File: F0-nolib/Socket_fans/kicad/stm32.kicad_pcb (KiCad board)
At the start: 2 copper layers, 93.5 x 55 mm, 67 parts, among them J1 A, J10 12v, J11 DB9_Male, J12 RS-485, J13 Conn_01x06, J2 B, J3 Conn_01x08_Female, J4 Conn_01x08_Female, J5 +/-, J6 CONN_02X03, J7 0/1, J8 2/3, J9 DB9_Female, P1 USB_A, P2 Hole, P3 Hole, P4 Hole, P5 Hole, Q1 SI2305, Q2 AO3407, SW1 SW_DIP_x01, U2 LM1117-5.0, U3 LM1117-3.3, U4 MCP2551-I/SN, U5 STM32F072CBTx, U6 MAX3485

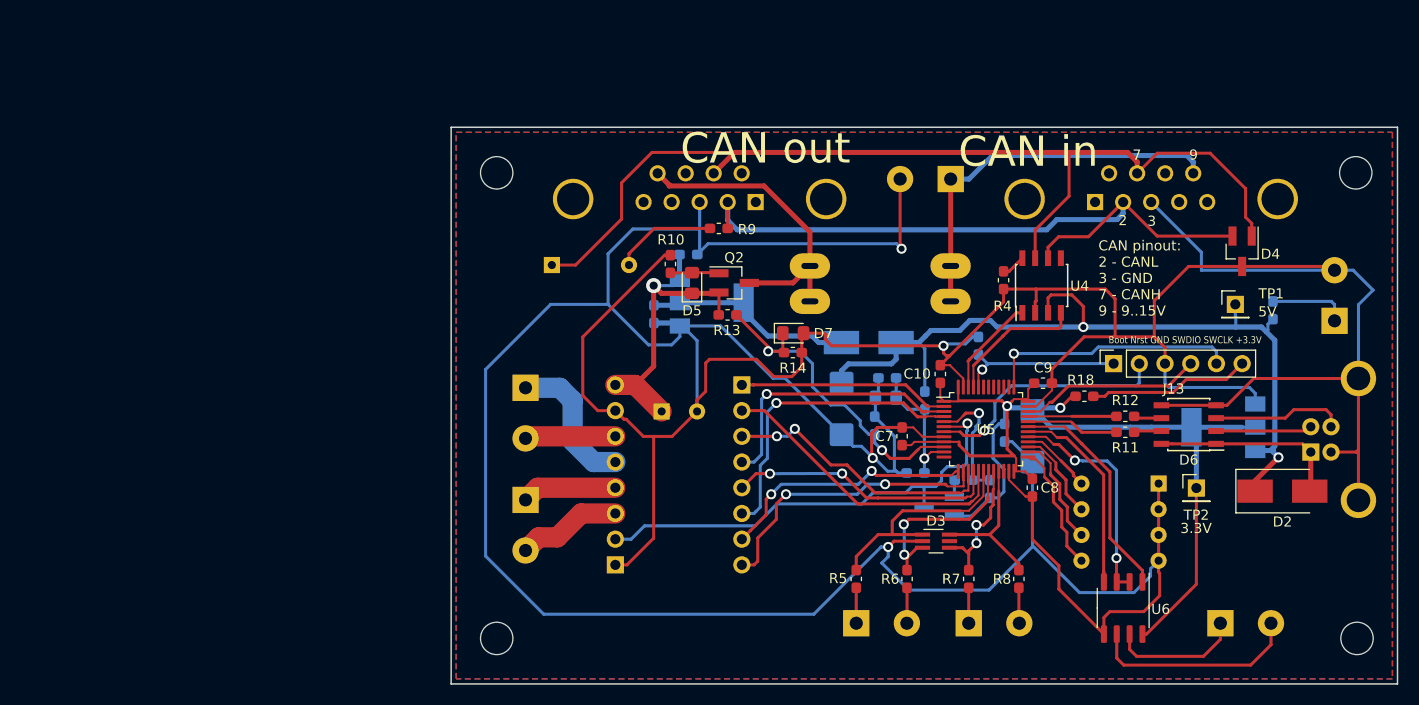
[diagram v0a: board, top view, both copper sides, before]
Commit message: add socket_fans PCB
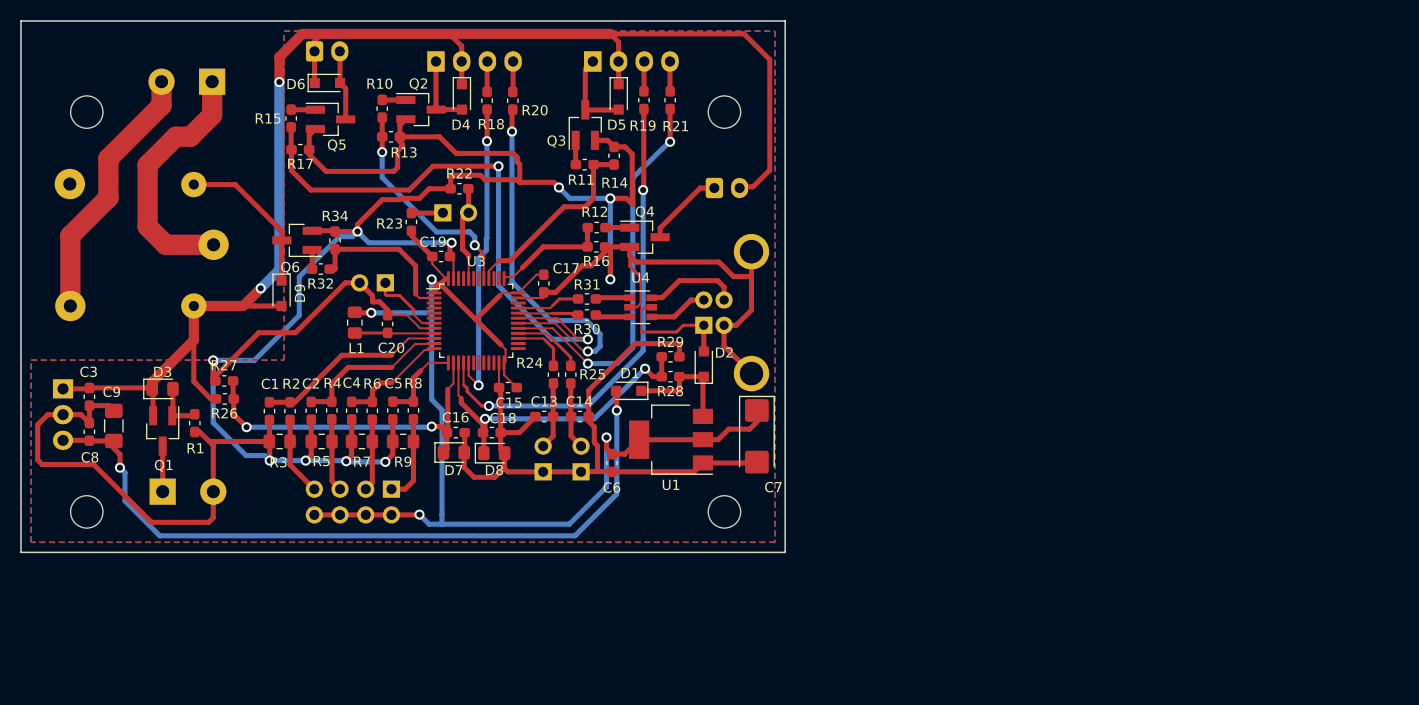
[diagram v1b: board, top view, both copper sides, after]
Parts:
- removed C10, C11, C12: 0.1, Capacitor_SMD:C_0603_1608Metric_Pad1.05x0.95mm_HandSolder
- removed F1: 1A, MyFootprints:FuseHolder
- removed J11: DB9_Male, Connector_Dsub:DSUB-9_Male_Horizontal_P2.77x2.84mm_EdgePinOffset4.94mm_Housed_MountingHolesOffset7.48mm
- removed J12: RS-485, TerminalBlock_Phoenix:TerminalBlock_Phoenix_MKDS-1,5-2_1x02_P5.00mm_Horizontal
- removed J13: Conn_01x06, Connector_PinSocket_2.54mm:PinSocket_1x06_P2.54mm_Vertical
- removed J9: DB9_Female, Connector_Dsub:DSUB-9_Female_Horizontal_P2.77x2.84mm_EdgePinOffset4.94mm_Housed_MountingHolesOffset7.48mm
- removed TP1, TP2: TestPoint, Connector_PinHeader_2.54mm:PinHeader_1x01_P2.54mm_Vertical
- removed U5: STM32F072CBTx, Package_QFP:LQFP-48_7x7mm_P0.5mm
- removed U6: MAX3485, Package_SO:SO-8_3.9x4.9mm_P1.27mm
- added C13: 0.1, Capacitor_SMD:C_0603_1608Metric_Pad1.05x0.95mm_HandSolder, F.Cu at (89.7, 91.1)
- added C14: 0.1, Capacitor_SMD:C_0603_1608Metric_Pad1.05x0.95mm_HandSolder, F.Cu at (93.2, 91.1)
- added C15: 0.1, Capacitor_SMD:C_0603_1608Metric_Pad1.05x0.95mm_HandSolder, F.Cu at (86.1, 88.2)
- added C16: 0.1, Capacitor_SMD:C_0603_1608Metric_Pad1.05x0.95mm_HandSolder, F.Cu at (81.0, 92.7)
- added C17: 0.1, Capacitor_SMD:C_0603_1608Metric_Pad1.05x0.95mm_HandSolder, F.Cu at (89.7, 77.9)
- added C18: 0.1, Capacitor_SMD:C_0603_1608Metric_Pad1.05x0.95mm_HandSolder, F.Cu at (84.5, 92.7)
- added C19: 0.1, Capacitor_SMD:C_0603_1608Metric_Pad1.05x0.95mm_HandSolder, F.Cu at (79.5, 75.3)
- added C20: 0.1, Capacitor_SMD:C_0603_1608Metric_Pad1.05x0.95mm_HandSolder, F.Cu at (74.2, 81.9)
- added D9: 1N5819, Diode_SMD:D_SOD-323_HandSoldering, F.Cu at (63.7, 78.9)
- added K1: SRD-12VDC, Relay_THT:Relay_SPDT_SANYOU_SRD_Series_Form_C, B.Cu at (57.0, 74.1)
- added L1: BMBA 0.1mH, Inductor_SMD:L_0805_2012Metric_Pad1.15x1.40mm_HandSolder, F.Cu at (71.0, 81.8)
- added Q3: IRLML2502, Package_TO_SOT_SMD:SOT-23_Handsoldering, F.Cu at (93.8, 62.3)
- added Q4: IRLML2502, Package_TO_SOT_SMD:SOT-23_Handsoldering, F.Cu at (99.6, 73.4)
- added Q5: IRLML2502, Package_TO_SOT_SMD:SOT-23_Handsoldering, F.Cu at (68.6, 61.7)
- added Q6: IRLML2502, Package_TO_SOT_SMD:SOT-23_Handsoldering, F.Cu at (65.3, 73.7)
- added R19: 510, Resistor_SMD:R_0603_1608Metric_Pad1.05x0.95mm_HandSolder, F.Cu at (99.5, 59.8)
- added R20: 510, Resistor_SMD:R_0603_1608Metric_Pad1.05x0.95mm_HandSolder, F.Cu at (86.6, 59.9)
- added R21: 510, Resistor_SMD:R_0603_1608Metric_Pad1.05x0.95mm_HandSolder, F.Cu at (102.1, 59.8)
- added R22: 47k, Resistor_SMD:R_0603_1608Metric_Pad1.05x0.95mm_HandSolder, F.Cu at (81.3, 68.6)
- added R23: 22, Resistor_SMD:R_0603_1608Metric_Pad1.05x0.95mm_HandSolder, F.Cu at (76.6, 71.9)
- added R24: 510, Resistor_SMD:R_0603_1608Metric_Pad1.05x0.95mm_HandSolder, F.Cu at (90.6, 86.9)
- added R25: 510, Resistor_SMD:R_0603_1608Metric_Pad1.05x0.95mm_HandSolder, F.Cu at (92.3, 86.9)
- added R26: 220k, Resistor_SMD:R_0603_1608Metric_Pad1.05x0.95mm_HandSolder, F.Cu at (58.1, 89.3)
- added R27: 56k, Resistor_SMD:R_0603_1608Metric_Pad1.05x0.95mm_HandSolder, F.Cu at (58.1, 87.6)
- added R28: 47k, Resistor_SMD:R_0603_1608Metric_Pad1.05x0.95mm_HandSolder, F.Cu at (102.2, 87.1)
- added R29: 47k, Resistor_SMD:R_0603_1608Metric_Pad1.05x0.95mm_HandSolder, F.Cu at (102.2, 85.2)
- added R30: 22, Resistor_SMD:R_0603_1608Metric_Pad1.05x0.95mm_HandSolder, F.Cu at (93.9, 81.0)
- added R31: 22, Resistor_SMD:R_0603_1608Metric_Pad1.05x0.95mm_HandSolder, F.Cu at (93.9, 79.5)
- added R32: 510, Resistor_SMD:R_0603_1608Metric_Pad1.05x0.95mm_HandSolder, F.Cu at (67.6, 76.5)
- added R34: 10k, Resistor_SMD:R_0603_1608Metric_Pad1.05x0.95mm_HandSolder, F.Cu at (69.0, 73.7)
- added SW2: SW_Push, Connector_PinSocket_2.54mm:PinSocket_1x02_P2.54mm_Vertical, B.Cu at (93.3, 96.5)
- added U1: LM1117-3.3, Package_TO_SOT_SMD:SOT-223-3_TabPin2, F.Cu at (102.2, 93.4)
- C1, C3, C5, R2: moved to F.Cu
- C2: value 100uF -> 0.1; footprint Capacitor_THT:CP_Radial_D8.0mm_P3.50mm -> Capacitor_SMD:C_0603_1608Metric_Pad1.05x0.95mm_HandSolder; moved to F.Cu
- C4, C6: value 47uF, 10V -> 0.1; footprint Capacitor_Tantalum_SMD:CP_EIA-6032-28_Kemet-C_Pad2.25x2.35mm_HandSolder -> Capacitor_SMD:C_0603_1608Metric_Pad1.05x0.95mm_HandSolder; moved to F.Cu
- C7: value 0.1 -> 47uF, 10V; footprint Capacitor_SMD:C_0603_1608Metric_Pad1.05x0.95mm_HandSolder -> Capacitor_Tantalum_SMD:CP_EIA-6032-28_Kemet-C_Pad2.25x2.35mm_HandSolder
- C9: value 0.1 -> 10uF, 10V; footprint Capacitor_SMD:C_0603_1608Metric_Pad1.05x0.95mm_HandSolder -> Capacitor_SMD:C_1206_3216Metric_Pad1.42x1.75mm_HandSolder
- D1: value MBRS130L -> 1N5819; footprint Diode_SMD:D_SMB_Handsoldering -> Diode_SMD:D_SOD-323_HandSoldering; moved to F.Cu
- D2: value MBRS130L -> 1N5819; footprint Diode_SMD:D_SMB_Handsoldering -> Diode_SMD:D_SOD-323_HandSoldering
- D3: value PESD3V3L4UG -> MM3Z7V5; footprint TO_SOT_Packages_SMD:SOT-363_SC-70-6_Handsoldering -> Diode_SMD:D_0805_2012Metric_Pad1.15x1.40mm_HandSolder
- D4: value PESD1CAN -> 1N5819; footprint TO_SOT_Packages_SMD:SOT-23_Handsoldering -> Diode_SMD:D_SOD-323_HandSoldering
- D5: value MM3Z7V5 -> 1N5819; footprint Diode_SMD:D_0805_2012Metric_Pad1.15x1.40mm_HandSolder -> Diode_SMD:D_SOD-323_HandSoldering
- D6: value USB6B1 -> 1N5819; footprint Package_SO:SOIC-8_3.9x4.9mm_P1.27mm -> Diode_SMD:D_SOD-323_HandSoldering
- D7: value MM3Z3V9 -> MM3Z4V7
- D8: value MM3Z3V9 -> MM3Z4V7; moved to F.Cu
- J1: value A -> 12VIN
- J10: value 12v -> Conn_01x02_Female; footprint TerminalBlock_Phoenix:TerminalBlock_Phoenix_MKDS-1,5-2_1x02_P5.00mm_Horizontal -> Connector_PinSocket_2.54mm:PinSocket_1x02_P2.54mm_Vertical
- J2: value B -> thermal; footprint TerminalBlock_Phoenix:TerminalBlock_Phoenix_MKDS-1,5-2_1x02_P5.00mm_Horizontal -> Connector_PinSocket_2.54mm:PinSocket_2x04_P2.54mm_Vertical
- J3: value Conn_01x08_Female -> Buzzer; footprint Connector_PinSocket_2.54mm:PinSocket_1x08_P2.54mm_Vertical -> Connector_JST:JST_EH_B2B-EH-A_1x02_P2.50mm_Vertical
- J4: value Conn_01x08_Female -> cooler3; footprint Connector_PinSocket_2.54mm:PinSocket_1x08_P2.54mm_Vertical -> Connector_JST:JST_EH_B2B-EH-A_1x02_P2.50mm_Vertical
- J5: value +/- -> FAN; footprint TerminalBlock_Phoenix:TerminalBlock_Phoenix_MKDS-1,5-2_1x02_P5.00mm_Horizontal -> Connector:FanPinHeader_1x04_P2.54mm_Vertical
- J6: value CONN_02X03 -> FAN; footprint Button_Switch_THT:SW_DIP_SPSTx04_Slide_9.78x12.34mm_W7.62mm_P2.54mm -> Connector:FanPinHeader_1x04_P2.54mm_Vertical
- J7: value 0/1 -> Conn_01x02_Female; footprint TerminalBlock_Phoenix:TerminalBlock_Phoenix_MKDS-1,5-2_1x02_P5.00mm_Horizontal -> Connector_PinSocket_2.54mm:PinSocket_1x02_P2.54mm_Vertical
- J8: value 2/3 -> MKDS
- P1: footprint Connectors_USB:USB_B_OST_USB-B1HSxx_Horizontal -> Connector_USB:USB_B_OST_USB-B1HSxx_Horizontal
- Q1: value SI2305 -> AO3401; footprint TO_SOT_Packages_SMD:SOT-23_Handsoldering -> Package_TO_SOT_SMD:SOT-23_Handsoldering; moved to F.Cu
- Q2: value AO3407 -> IRLML2502; footprint TO_SOT_Packages_SMD:SOT-23_Handsoldering -> Package_TO_SOT_SMD:SOT-23_Handsoldering
- R1: value 330 -> 10k; moved to F.Cu
- R10: value 10k -> 510
- R11, R12, R18: value 22 -> 510
- R13: value 220k -> 10k
- R14: value 56k -> 10k
- R15: value 47k -> 510; moved to F.Cu
- R16, R17: value 47k -> 10k; moved to F.Cu
- R3: value 120 -> 4k7, 1%; footprint Resistor_SMD:R_0603_1608Metric_Pad1.05x0.95mm_HandSolder -> Resistor_SMD:R_0805_2012Metric_Pad1.15x1.40mm_HandSolder; moved to F.Cu
- R4: value 15k -> 10k
- R5, R7: value 330 -> 4k7, 1%; footprint Resistor_SMD:R_0603_1608Metric_Pad1.05x0.95mm_HandSolder -> Resistor_SMD:R_0805_2012Metric_Pad1.15x1.40mm_HandSolder
- R6, R8: value 330 -> 10k
- R9: value 120 -> 4k7, 1%; footprint Resistor_SMD:R_0603_1608Metric_Pad1.05x0.95mm_HandSolder -> Resistor_SMD:R_0805_2012Metric_Pad1.15x1.40mm_HandSolder
- SW1: value SW_DIP_x01 -> SW_Push; footprint Button_Switch_THT:SW_DIP_SPSTx01_Slide_6.7x4.1mm_W7.62mm_P2.54mm_LowProfile -> Connector_PinSocket_2.54mm:PinSocket_1x02_P2.54mm_Vertical
- U2: value LM1117-5.0 -> L7805; footprint TO_SOT_Packages_SMD:SOT-223-3_TabPin2 -> Package_TO_SOT_THT:TO-220-3_Vertical
- U3: value LM1117-3.3 -> STM32F072CBTx; footprint TO_SOT_Packages_SMD:SOT-223-3_TabPin2 -> Package_QFP:LQFP-48_7x7mm_P0.5mm; moved to F.Cu
- U4: value MCP2551-I/SN -> USBLC6-2SC6; footprint Package_SO:SOIC-8_3.9x4.9mm_P1.27mm -> Package_TO_SOT_SMD:SOT-23-6
- moved P4 125.5 mm to (44.5, 61.0)
- moved R3 99.0 mm to (63.6, 93.5), turned to 0 degrees
- moved C8 93.3 mm to (44.8, 92.6)
- moved J5 92.4 mm to (79.0, 56.0), turned to 0 degrees
- moved J8 91.9 mm to (56.9, 58.0), turned to 180 degrees
- moved C9 91.9 mm to (47.2, 92.0), turned to 90 degrees
- moved D6 91.5 mm to (68.3, 58.1), turned to 0 degrees
- moved D4 78.6 mm to (81.6, 59.5)
- moved D3 77.9 mm to (52.0, 88.3)
- moved Q1 77.1 mm to (52.0, 92.5), turned to 270 degrees
- moved R1 76.2 mm to (55.2, 91.7), turned to 270 degrees
- moved U3 74.6 mm to (83.0, 81.6), turned to 0 degrees
- moved J6 69.7 mm to (94.5, 56.0), turned to 0 degrees
- moved R17 69.7 mm to (65.6, 64.7), turned to 180 degrees
- moved R2 69.6 mm to (64.6, 90.5)
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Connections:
- C1 pad 1: /12Vin -> GND
- C1 pad 2: GND -> /ADC0
- C2 pad 1: /12Vin -> GND
- C2 pad 2: GND -> /ADC1
- C3 pad 1: /5Vin -> +12V
- C4 pad 1: +5V -> GND
- C4 pad 2: GND -> /ADC2
- C5 pad 1: +3V3 -> GND
- C5 pad 2: GND -> /ADC3
- C7 pad 1: GND -> +3V3
- C7 pad 2: +3V3 -> GND
- C8 pad 1: GND -> /5Vin
- C8 pad 2: +3V3 -> GND
- C9 pad 1: GND -> /5Vin
- C9 pad 2: +3V3 -> GND
- D3 pad 1: /ESW0 -> +12V
- D3 pad 2: GND -> Net-(D3-Pad2)
- D4 pad 1: Net-(D4-Pad1) -> +12V
- D5 pad 1: /12Vin -> +12V
- D6 pad 1: /5Vusb -> +12V
- J1 pad 2: Net-(J1-Pad2) -> GND
- J10 pad 1: Net-(F1-Pad1) -> /NRST
- J2 pad 2: Net-(J2-Pad2) -> +3V3
- J3 pad 1: GND -> Net-(J3-Pad1)
- J3 pad 2: /~FAULT -> +12V
- J4 pad 1: /~EN -> +12V
- J4 pad 2: /MOSI -> Net-(D6-Pad2)
- J5 pad 1: Net-(J5-Pad1) -> Net-(D4-Pad2)
- J5 pad 2: GND -> +12V
- J6 pad 1: GND -> Net-(D5-Pad2)
- J6 pad 2: GND -> +12V
- J6 pad 3: GND -> Net-(J6-Pad3)
- J6 pad 4: GND -> Net-(J6-Pad4)
- J7 pad 2: Net-(J7-Pad2) -> /BOOT0
- P1 pad 2: Net-(D6-Pad2) -> Net-(P1-Pad2)
- P1 pad 3: Net-(D6-Pad3) -> Net-(P1-Pad3)
- Q1 pad 1: Net-(Q1-Pad1) -> Net-(D3-Pad2)
- Q1 pad 2: +3V3 -> +12V
- Q1 pad 3: /~FAULT -> Net-(J1-Pad1)
- Q2 pad 1: Net-(D5-Pad2) -> Net-(Q2-Pad1)
- Q2 pad 2: /12Vin -> GND
- Q2 pad 3: Net-(F1-Pad2) -> Net-(D4-Pad2)
- R1 pad 1: Net-(Q1-Pad1) -> Net-(D3-Pad2)
- R1 pad 2: /VIO_on -> GND
- R10 pad 1: Net-(D5-Pad2) -> Net-(Q2-Pad1)
- R10 pad 2: GND -> /Cooler1
- R11 pad 1: Net-(D6-Pad7) -> Net-(Q3-Pad1)
- R11 pad 2: Net-(R11-Pad2) -> /Cooler0
- R12 pad 1: Net-(D6-Pad6) -> Net-(Q4-Pad1)
- R12 pad 2: Net-(R12-Pad2) -> /Buzzer
- R13 pad 1: /12Vin -> GND
- R13 pad 2: /AIN0 -> /Cooler1
- R14 pad 1: /AIN0 -> GND
- R14 pad 2: GND -> /Cooler0
- R15 pad 1: +5V -> Net-(Q5-Pad1)
- R15 pad 2: /AIN1 -> /TIM1_CH3
- R16 pad 1: /AIN1 -> GND
- R16 pad 2: GND -> /Buzzer
- R17 pad 1: /BOOT0 -> GND
- R17 pad 2: GND -> /TIM1_CH3
- R18 pad 1: Net-(J13-Pad6) -> /TIM14_CH1
- R18 pad 2: +3V3 -> Net-(J5-Pad3)
- R2 pad 1: +3V3 -> Net-(J2-Pad7)
- R2 pad 2: /VIO_on -> /ADC0
- R3 pad 1: +5V -> GND
- R3 pad 2: Net-(J5-Pad1) -> Net-(J2-Pad7)
- R4 pad 1: Net-(R4-Pad1) -> Net-(J2-Pad5)
- R4 pad 2: GND -> /ADC1
- R5 pad 1: /ESW0 -> GND
- R5 pad 2: Net-(J7-Pad1) -> Net-(J2-Pad5)
- R6 pad 1: /ESW1 -> Net-(J2-Pad3)
- R6 pad 2: Net-(J7-Pad2) -> /ADC2
- R7 pad 1: /ESW2 -> GND
- R7 pad 2: Net-(J8-Pad1) -> Net-(J2-Pad3)
- R8 pad 1: /ESW3 -> Net-(J2-Pad1)
- R8 pad 2: Net-(J8-Pad2) -> /ADC3
- R9 pad 1: Net-(R9-Pad1) -> GND
- R9 pad 2: Net-(D4-Pad2) -> Net-(J2-Pad1)
- SW1 pad 1: Net-(D4-Pad1) -> GND
- SW1 pad 2: Net-(R9-Pad1) -> Net-(C13-Pad1)
- U2 pad 1: GND -> +12V
- U2 pad 2: /5Vin -> GND
- U2 pad 3: /12Vin -> /5Vin
- U3 pad 1: GND -> +3V3
- U3 pad 2: +3V3 -> /Relay
- U3 pad 3: +5V -> (no net)
- U4 pad 1: /CAN_Tx -> Net-(R31-Pad1)
- U4 pad 3: +5V -> Net-(R30-Pad1)
- U4 pad 4: /CAN_Rx -> Net-(P1-Pad2)
- U4 pad 5: (no net) -> /5Vusb
- U4 pad 6: Net-(D4-Pad2) -> Net-(P1-Pad3)
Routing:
- net +12V: track 0.00 -> 181.0 mm, vias 0 -> 2
- net GND: track 531.3 -> 365.3 mm, vias 4 -> 10
- net Net-(D4-Pad1): track 98.8 -> 0.00 mm
- net +5V: track 82.3 -> 11.5 mm, vias 2 -> 0
- net Net-(D4-Pad2): track 68.2 -> 7.30 mm
- net /TIM1_CH3: track 0.00 -> 57.1 mm, vias 0 -> 2
- net /5Vin: track 20.8 -> 73.4 mm, vias 0 -> 2
- net /TIM3_CH1: track 0.00 -> 47.1 mm, vias 0 -> 2
- net /~FAULT: track 46.8 -> 0.00 mm, vias 1 -> 0
- net /TIM1_CH1: track 0.00 -> 38.6 mm, vias 0 -> 2
- net /TIM1_CH2: track 0.00 -> 38.5 mm, vias 0 -> 2
- net Net-(F1-Pad1): track 38.4 -> 0.00 mm
- net Net-(F1-Pad2): track 31.1 -> 0.00 mm
- net /12Vin: track 30.6 -> 0.00 mm, vias 1 -> 0
- net /TIM14_CH1: track 0.00 -> 30.2 mm, vias 0 -> 2
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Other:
- board size 93.5 x 55 mm -> 75.5 x 52.5 mm
- board text removed: "+12V"
- board text removed: "+4V"
- board text removed: "1 0"
- board text removed: "1 <> 0"
- board text removed: "1B 2B 1A 2A"
- board text removed: "2"
- board text removed: "3"
- board text removed: "3 2"
- board text removed: "3 2 1 0"
- board text removed: "3.3V"
- board text removed: "5V"
- board text removed: "7"
- board text removed: "9"
- board text removed: "A B"
- board text removed: "ADDR"
- board text removed: "Boot Nrst GND SWDIO SWCLK +3.3V"
- board text removed: "C2"
- board text removed: "CAN in"
- board text removed: "CAN out"
- board text removed: "CAN pinout: 2 - CANL 3 - GND 7 - CANH 9 - 9..15V"
- board text removed: "DIR"
- board text removed: "ESW"
- board text removed: "ESW POW"
- board text removed: "GND"
- board text removed: "MOTOR"
- board text removed: "RS-485"
- board text removed: "Terminator"
- board text removed: "Vmot"
- board text removed: "~EN"

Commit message: Add pre-alpha version of Socket_fans code
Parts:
- removed D8: MM3Z4V7, Diode_SMD:D_0805_2012Metric_Pad1.15x1.40mm_HandSolder
- added C10: 47u, Capacitor_THT:CP_Radial_D8.0mm_P3.50mm, B.Cu at (63.8, 82.7)
- D7: value MM3Z4V7 -> MM3Z4V3
- R26: value 220k -> 3.3k
- R27: value 56k -> 1k
- R28, R29: value 47k -> 4.7k
- turned D9 to 90 degrees
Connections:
- D9 pad 1: Net-(D9-Pad1) -> +12V
- D9 pad 2: +12V -> Net-(D9-Pad2)
- K1 pad 5: Net-(D9-Pad1) -> Net-(D9-Pad2)
- Q6 pad 3: Net-(D9-Pad1) -> Net-(D9-Pad2)
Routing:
- net Net-(D9-Pad2): track 0.00 -> 17.0 mm
- net Net-(D9-Pad1): track 15.5 -> 0.00 mm
- net GND: track 365.3 -> 370.9 mm
- net +12V: track 181.0 -> 185.1 mm
- net /AIN1: track 33.2 -> 31.2 mm
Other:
- board text added: "+Buzzer"
- board text added: "-12V+"
- board text added: "0"
- board text added: "1"
- board text added: "2"
- board text added: "220V"
- board text added: "3"
- board text added: "Btn0"
- board text added: "Btn1"
- board text added: "Cooler 0"
- board text added: "Cooler 1"
- board text added: "Cooler 2"

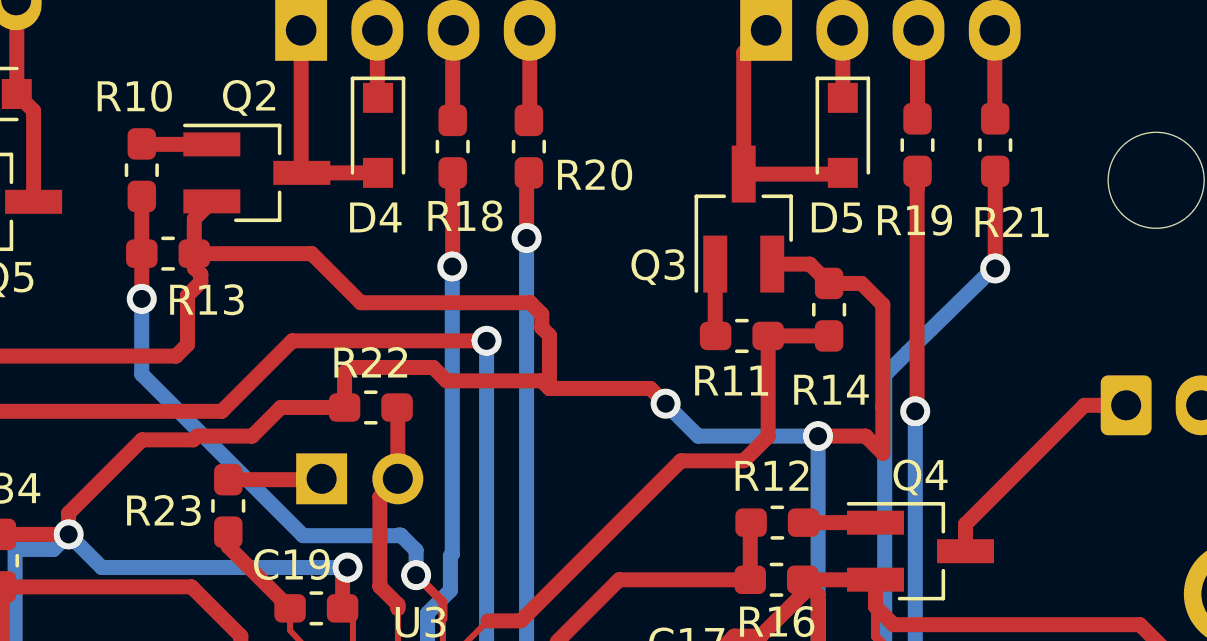
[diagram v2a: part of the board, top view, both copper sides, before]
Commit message: fixed schematics of socket_fans
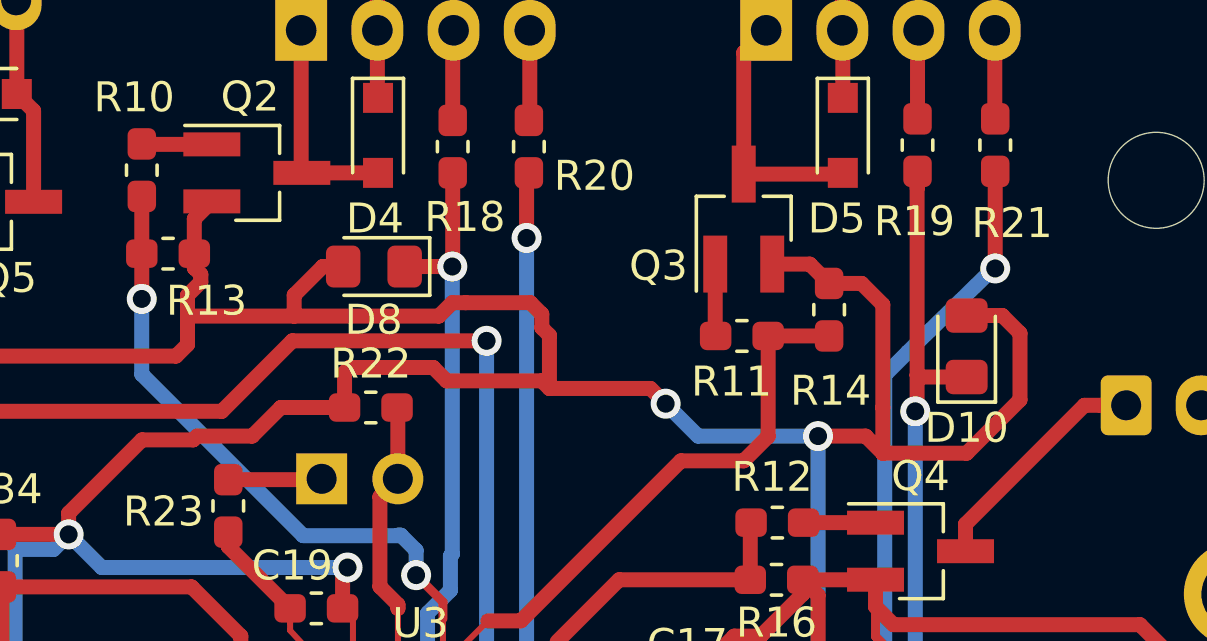
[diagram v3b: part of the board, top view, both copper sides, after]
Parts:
- added D10: MM3Z3V6, Diode_SMD:D_0805_2012Metric_Pad1.15x1.40mm_HandSolder, F.Cu at (101.2, 66.5)
- added D8: MM3Z3V6, Diode_SMD:D_0805_2012Metric_Pad1.15x1.40mm_HandSolder, F.Cu at (81.4, 63.9)
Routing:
- net GND: track 370.9 -> 382.9 mm
- net /TIM3_CH1: track 47.1 -> 48.8 mm
- net /TIM14_CH1: track 30.2 -> 31.8 mm
